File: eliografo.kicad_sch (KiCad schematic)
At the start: 46 parts, among them J10 Conn_01x03, J11 Conn_01x02, J3 Conn_01x05, J4 Conn_01x05, J5 Conn_02x06_Odd_Even, J6 Conn_01x02, J7 Conn_01x02, J8 Conn_01x03, J9 Conn_01x03, Q1 IRF540N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

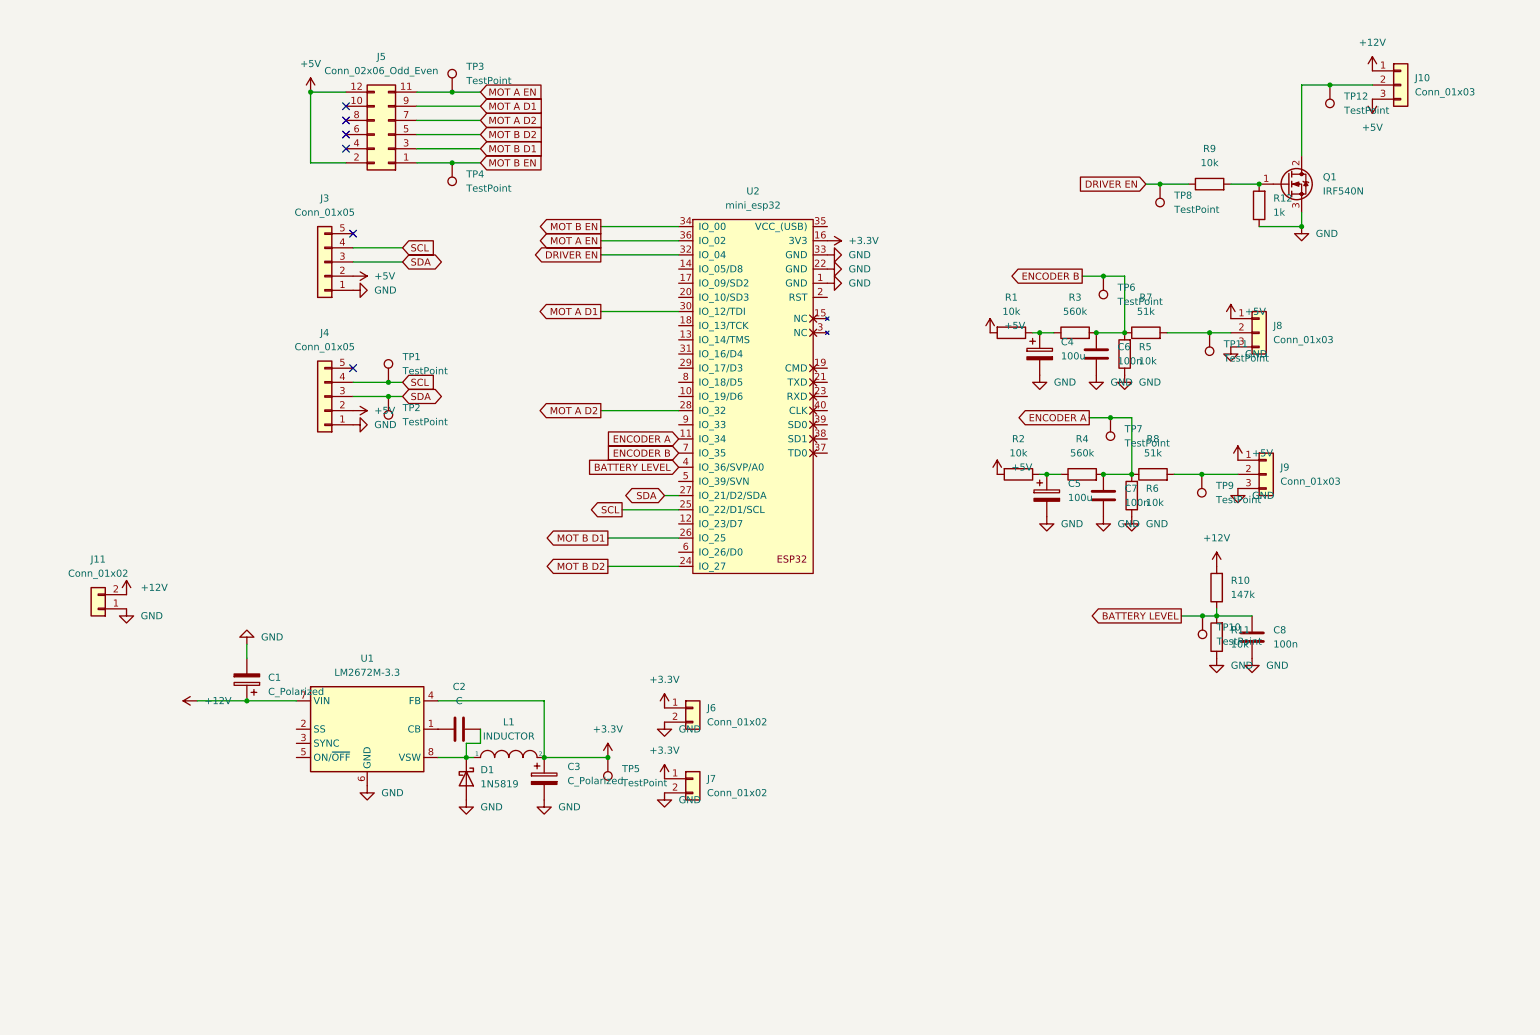
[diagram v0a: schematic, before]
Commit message: Modifications added in debug of v0.1
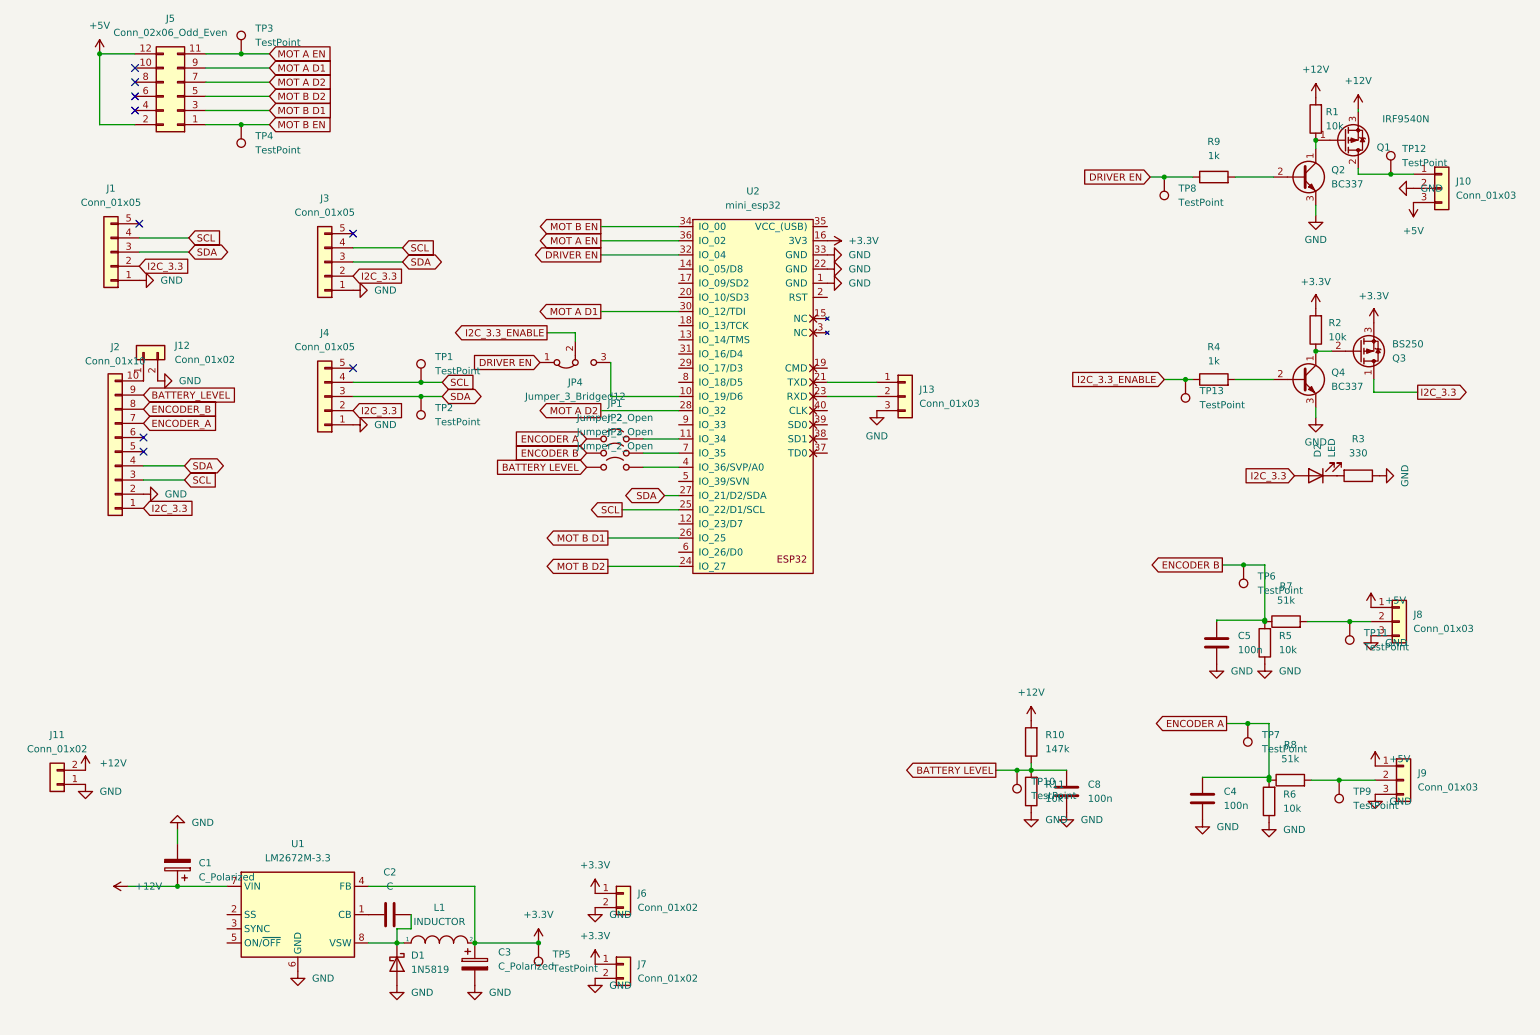
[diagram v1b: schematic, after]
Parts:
- removed C4, C5: 100u, Capacitor_THT:CP_Radial_D8.0mm_P5.00mm, symbol Device:C_Polarized
- removed C6, C7: 100n, Capacitor_THT:C_Rect_L7.0mm_W2.0mm_P5.00mm, symbol Device:C
- removed Q1: IRF540N, Package_TO_SOT_THT:TO-220-3_Vertical, symbol Transistor_FET:IRF540N
- removed R12: 1k, Resistor_THT:R_Axial_DIN0204_L3.6mm_D1.6mm_P5.08mm_Horizontal, symbol Device:R
- added C4, C5: 100n, Capacitor_THT:C_Rect_L7.0mm_W2.0mm_P5.00mm, symbol Device:C
- added D2: LED, symbol Device:LED
- added J1: Conn_01x05, Connector_PinHeader_2.54mm:PinHeader_1x05_P2.54mm_Vertical, symbol Connector_Generic:Conn_01x05
- added J12: Conn_01x02, Connector_Phoenix_MSTB:PhoenixContact_MSTBA_2,5_2-G-5,08_1x02_P5.08mm_Horizontal, symbol Connector_Generic:Conn_01x02
- added J13: Conn_01x03, symbol Connector_Generic:Conn_01x03
- added J2: Conn_01x10, symbol Connector_Generic:Conn_01x10
- added JP1, JP2, JP3: Jumper_2_Open, symbol Jumper:Jumper_2_Open
- added JP4: Jumper_3_Bridged12, symbol Jumper:Jumper_3_Bridged12
- added Q1: IRF9540N, Package_TO_SOT_THT:TO-220-3_Vertical, symbol Transistor_FET:IRF9540N
- added Q2, Q4: BC337, Package_TO_SOT_THT:TO-92_Inline, symbol Transistor_BJT:BC337
- added Q3: BS250, Package_TO_SOT_THT:TO-92_Inline, symbol Transistor_FET:BS250
- added TP13: TestPoint, TestPoint:TestPoint_THTPad_D2.0mm_Drill1.0mm, symbol Connector:TestPoint
- R3: value 560k -> 330
- R4: value 560k -> 1k
- R9: value 10k -> 1k
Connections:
- net +12V: now also R1.2, Q1.3 (S); no longer J10.1 (Pin_1)
- net +3.3V: now also R2.2, Q3.3 (S)
- net +5V: no longer J3.2 (Pin_2), J4.2 (Pin_2), R1.2, R2.2
- net BATTERY LEVEL: now also JP3.1 (A); no longer U2.4 (IO_36/SVP/A0)
- net DRIVER EN: now also JP4.1 (A)
- net ENCODER A: now also C4.1, JP1.1 (A); no longer R4.2, U2.11 (IO_34)
- net ENCODER B: now also C5.1, JP2.1 (A); no longer R3.2, U2.7 (IO_35)
- net GND: now also J10.2 (Pin_2), R3.1, C4.2, C5.2, J1.1 (Pin_1), J12.2 (Pin_2), J13.3 (Pin_3), J2.2 (Pin_2), Q2.3 (E), Q4.3 (E)
- net SCL: now also J1.4 (Pin_4), J2.3 (Pin_3)
- net SDA: now also J1.3 (Pin_3), J2.4 (Pin_4)
- net at TP12.1: now also J10.1 (Pin_1), Q1.2 (D); no longer J10.2 (Pin_2)
- net at R9.2: now also Q2.2 (B)
- net at R1.1: now also Q1.1 (G), Q2.1 (C); no longer R3.1
- net at R2.1: now also Q3.2 (G), Q4.1 (C); no longer R4.1
- net at U2.10 (IO_19/D6): now also JP4.3 (B)
- net at U2.21 (TXD): now also J13.1 (Pin_1)
- net at U2.23 (RXD): now also J13.2 (Pin_2)
- new net: D2.1 (K), R3.2
- new net: J12.1 (Pin_1), J2.10 (Pin_10)
- new net: JP2.2 (B), U2.7 (IO_35)
- new net: JP3.2 (B), U2.4 (IO_36/SVP/A0)
- new net: Q4.2 (B), R4.2
- new net: JP1.2 (B), U2.11 (IO_34)
- new net BATTERY_LEVEL: J2.9 (Pin_9)
- new net ENCODER_A: J2.7 (Pin_7)
- new net ENCODER_B: J2.8 (Pin_8)
- new net I2C_3.3: D2.2 (A), J1.2 (Pin_2), J2.1 (Pin_1), J3.2 (Pin_2), J4.2 (Pin_2), Q3.1 (D)
- new net I2C_3.3_ENABLE: JP4.2 (C), R4.1, TP13.1
- no-connect marks 6 -> 9
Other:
- moved on the sheet: C1, C2, C3, C8, D1, J10, J11, J5, J6, J7, J8, J9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

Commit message: First sketch of version 0.2
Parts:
- removed D1: 1N5819, Diode_THT:D_DO-41_SOD81_P10.16mm_Horizontal, symbol Diode:1N5819
- removed Q2, Q4: BC337, Package_TO_SOT_THT:TO-92_Inline, symbol Transistor_BJT:BC337
- removed Q3: BS250, Package_TO_SOT_THT:TO-92_Inline, symbol Transistor_FET:BS250
- added D1: SB140, Diode_SMD:D_SMA, symbol Diode:B140-E3
- added H2, H3, H4, H5, H6: MountingHole_Pad, MountingHole:MountingHole_3.2mm_M3_Pad, symbol Mechanical:MountingHole_Pad
- added JP5: LED EN, Connector_PinHeader_2.54mm:PinHeader_1x02_P2.54mm_Vertical, symbol Jumper:Jumper_2_Open
- added Q2, Q4: MMBT3904, Package_TO_SOT_SMD:SOT-23, symbol Transistor_BJT:MMBT3904
- added Q5: IRLML9301, Package_TO_SOT_SMD:SOT-23, symbol Transistor_FET:IRLML9301
- C1: value C_Polarized -> 100uF 25V; footprint Capacitor_THT:CP_Radial_D8.0mm_P5.00mm -> Capacitor_Tantalum_SMD:CP_EIA-7361-38_AVX-V_HandSolder
- C2, C4, C5, C8: footprint Capacitor_THT:C_Rect_L7.0mm_W2.0mm_P5.00mm -> Capacitor_SMD:C_0805_2012Metric_Pad1.18x1.45mm_HandSolder
- C3: value C_Polarized -> 100uF 10V; footprint Capacitor_THT:CP_Radial_D8.0mm_P5.00mm -> Capacitor_Tantalum_SMD:CP_EIA-7343-15_Kemet-W_HandSolder
- D2: footprint (none) -> LED_THT:LED_D3.0mm
- J1, J3, J4: footprint Connector_PinHeader_2.54mm:PinHeader_1x05_P2.54mm_Vertical -> Connector_PinSocket_2.54mm:PinSocket_1x05_P2.54mm_Vertical
- J10: value Conn_01x03 -> Driver PSU; footprint Connector_Phoenix_MSTB:PhoenixContact_MSTBA_2,5_3-G-5,08_1x03_P5.08mm_Horizontal -> TerminalBlock_Phoenix:TerminalBlock_Phoenix_MKDS-1,5-3-5.08_1x03_P5.08mm_Horizontal
- J11: value Conn_01x02 -> POWER SUPPLY; footprint Connector_Phoenix_MSTB:PhoenixContact_MSTBA_2,5_2-G-5,08_1x02_P5.08mm_Horizontal -> TerminalBlock_Phoenix:TerminalBlock_Phoenix_MKDS-1,5-2-5.08_1x02_P5.08mm_Horizontal
- J12: value Conn_01x02 -> EXTRA ADC; footprint Connector_Phoenix_MSTB:PhoenixContact_MSTBA_2,5_2-G-5,08_1x02_P5.08mm_Horizontal -> Connector_PinHeader_2.54mm:PinHeader_1x02_P2.54mm_Vertical
- J13: footprint (none) -> Connector_PinHeader_2.54mm:PinHeader_1x03_P2.54mm_Vertical
- J2: value Conn_01x10 -> ADC; footprint (none) -> Connector_PinSocket_2.54mm:PinSocket_1x10_P2.54mm_Vertical
- J5: value Conn_02x06_Odd_Even -> MotorDriver; footprint Connector_PinHeader_2.54mm:PinHeader_2x06_P2.54mm_Vertical -> Connector_IDC:IDC-Header_2x06_P2.54mm_Vertical
- J8: value Conn_01x03 -> Encoder ALT; footprint Connector_Phoenix_MSTB:PhoenixContact_MSTBA_2,5_3-G-5,08_1x03_P5.08mm_Horizontal -> TerminalBlock_Phoenix:TerminalBlock_Phoenix_MKDS-1,5-3-5.08_1x03_P5.08mm_Horizontal
- J9: value Conn_01x03 -> Encoder AZI; footprint Connector_Phoenix_MSTB:PhoenixContact_MSTBA_2,5_3-G-5,08_1x03_P5.08mm_Horizontal -> TerminalBlock_Phoenix:TerminalBlock_Phoenix_MKDS-1,5-3-5.08_1x03_P5.08mm_Horizontal
- JP1: value Jumper_2_Open -> ENC AZI DIRECT; footprint (none) -> Connector_PinHeader_2.54mm:PinHeader_1x02_P2.54mm_Vertical
- JP2: value Jumper_2_Open -> ENC ALT DIRECT; footprint (none) -> Connector_PinHeader_2.54mm:PinHeader_1x02_P2.54mm_Vertical
- JP3: value Jumper_2_Open -> BATT DIRECT; footprint (none) -> Connector_PinHeader_2.54mm:PinHeader_1x02_P2.54mm_Vertical
- JP4: value Jumper_3_Bridged12 -> I2C ENABLE; footprint (none) -> Connector_PinHeader_2.54mm:PinHeader_1x03_P2.54mm_Vertical
- L1: value INDUCTOR -> 47uH; footprint Inductor_THT:L_Axial_L20.3mm_D12.1mm_P7.62mm_Vertical_Vishay_IHA-101 -> Inductor_SMD:L_Coilcraft_XAL6060-XXX
- Q1: footprint Package_TO_SOT_THT:TO-220-3_Vertical -> Package_TO_SOT_SMD:TO-252-3_TabPin2
- R1, R10, R11, R2, R3, R4, R5, R6, R7, R8, R9: footprint Resistor_THT:R_Axial_DIN0204_L3.6mm_D1.6mm_P5.08mm_Horizontal -> Resistor_SMD:R_0805_2012Metric_Pad1.20x1.40mm_HandSolder
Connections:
- net +3.3V: now also Q5.2 (S)
- net GND: now also D1.2 (A), Q2.2 (E), Q4.2 (E)
- net I2C_3.3: now also JP5.1 (A), Q5.3 (D); no longer D2.2 (A)
- net +12 DRIVER: now reaches J10.1 (Pin_1), Q1.2 (D), TP12.1
- net at Q1.1 (G), R1.1: now also Q2.3 (C)
- net at C2.2, L1.1, U1.8 (VSW): now also D1.1 (K)
- net at R2.1: now also Q4.3 (C), Q5.1 (G)
- net at R4.2: now also Q4.1 (B)
- net at R9.2: now also Q2.1 (B)
- new net: D2.2 (A), JP5.2 (B)
- no-connect marks 9 -> 12

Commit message: Version 0.2 ready for production
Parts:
- removed TP1, TP10, TP13, TP2, TP6, TP7: TestPoint, TestPoint:TestPoint_THTPad_D2.0mm_Drill1.0mm, symbol Connector:TestPoint
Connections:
- net BATTERY_LEVEL is gone; now on net BATTERY LEVEL: J2.9 (Pin_9)
- net ENCODER_A is gone; now on net ENCODER A: J2.7 (Pin_7)
- net ENCODER_B is gone; now on net ENCODER B: J2.8 (Pin_8)
